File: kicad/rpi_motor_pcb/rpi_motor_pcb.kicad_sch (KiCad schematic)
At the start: 15 parts, among them J1 Raspberry_Pi_2_3, J4 PWR IN, J9 LSW1

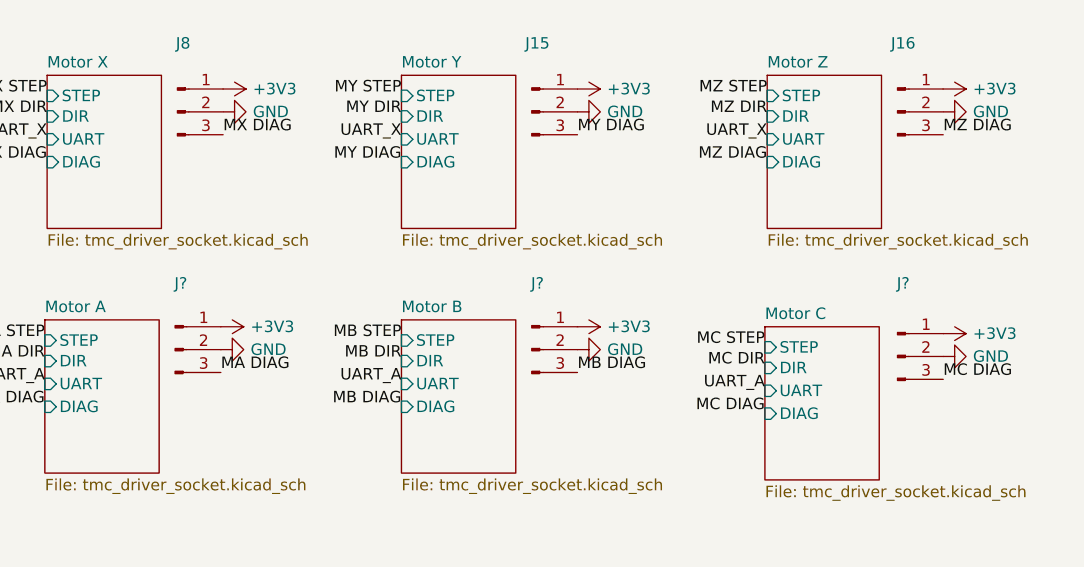
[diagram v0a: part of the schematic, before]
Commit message: rpi_motor_pcb: a,b,c endstops
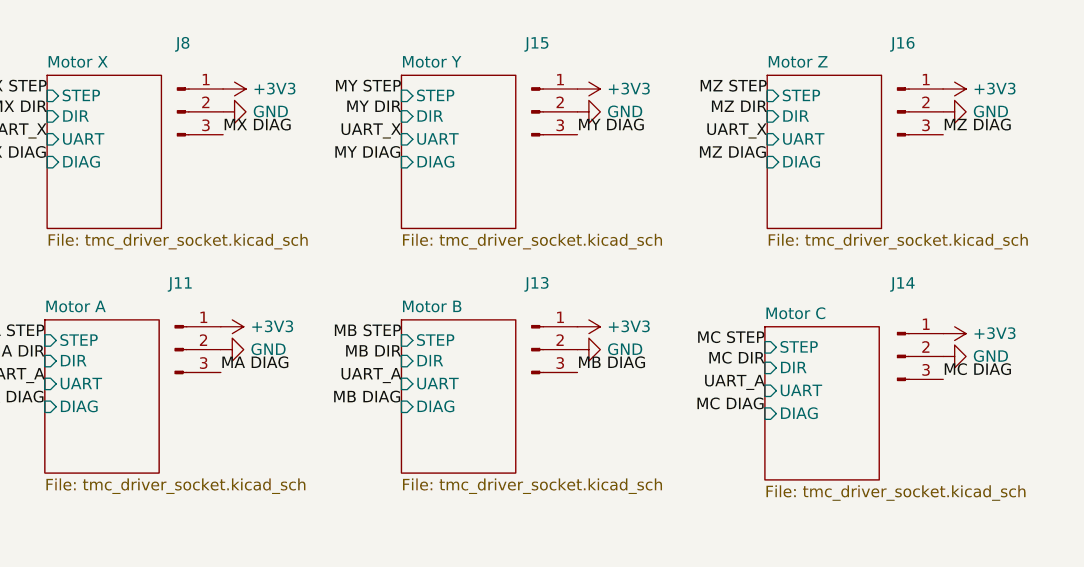
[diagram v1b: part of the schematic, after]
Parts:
- gave numbers to parts that had none: 3
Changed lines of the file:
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@@
   (symbol (lib_id "power:+3V3") (at 200.66 51.308 270) (unit 1)
     (in_bom yes) (on_board yes) (fields_autoplaced)
-    (property "Reference" "#PWR?" (id 0) (at 196.85 51.308 0)
+    (property "Reference" "#PWR091" (id 0) (at 196.85 51.308 0)
       (effects (font (size 1.27 1.27)) hide)
     )
@@
   (symbol (lib_id "power:+3V3") (at 120.396 50.546 270) (unit 1)
     (in_bom yes) (on_board yes) (fields_autoplaced)
-    (property "Reference" "#PWR?" (id 0) (at 116.586 50.546 0)
+    (property "Reference" "#PWR087" (id 0) (at 116.586 50.546 0)
       (effects (font (size 1.27 1.27)) hide)
     )
@@
   (symbol (lib_id "power:GND") (at 200.66 53.848 90) (unit 1)
     (in_bom yes) (on_board yes) (fields_autoplaced)
-    (property "Reference" "#PWR?" (id 0) (at 207.01 53.848 0)
+    (property "Reference" "#PWR092" (id 0) (at 207.01 53.848 0)
       (effects (font (size 1.27 1.27)) hide)
     )
@@
   (symbol (lib_id "power:GND") (at 160.02 53.086 90) (unit 1)
     (in_bom yes) (on_board yes) (fields_autoplaced)
-    (property "Reference" "#PWR?" (id 0) (at 166.37 53.086 0)
+    (property "Reference" "#PWR090" (id 0) (at 166.37 53.086 0)
       (effects (font (size 1.27 1.27)) hide)
     )
@@
   (symbol (lib_id "Connector:Conn_01x03_Male") (at 195.58 53.848 0) (unit 1)
     (in_bom yes) (on_board yes) (fields_autoplaced)
-    (property "Reference" "J?" (id 0) (at 196.215 45.72 0))
+    (property "Reference" "J14" (id 0) (at 196.215 45.72 0))
     (property "Value" "" (id 1) (at 196.215 48.26 0))
     (property "Footprint" "Connector_PinHeader_2.54mm:PinHeader_1x03_P2.54mm_Vertical" (id 2) (at 195.58 53.848 0)
@@
   (symbol (lib_id "power:GND") (at 120.396 53.086 90) (unit 1)
     (in_bom yes) (on_board yes) (fields_autoplaced)
-    (property "Reference" "#PWR?" (id 0) (at 126.746 53.086 0)
+    (property "Reference" "#PWR088" (id 0) (at 126.746 53.086 0)
       (effects (font (size 1.27 1.27)) hide)
     )
@@
   (symbol (lib_id "power:+3V3") (at 160.02 50.546 270) (unit 1)
     (in_bom yes) (on_board yes) (fields_autoplaced)
-    (property "Reference" "#PWR?" (id 0) (at 156.21 50.546 0)
+    (property "Reference" "#PWR089" (id 0) (at 156.21 50.546 0)
       (effects (font (size 1.27 1.27)) hide)
     )
@@
   (symbol (lib_id "Connector:Conn_01x03_Male") (at 154.94 53.086 0) (unit 1)
     (in_bom yes) (on_board yes) (fields_autoplaced)
-    (property "Reference" "J?" (id 0) (at 155.575 45.72 0))
+    (property "Reference" "J13" (id 0) (at 155.575 45.72 0))
     (property "Value" "" (id 1) (at 155.575 48.26 0))
     (property "Footprint" "Connector_PinHeader_2.54mm:PinHeader_1x03_P2.54mm_Vertical" (id 2) (at 154.94 53.086 0)
@@
   (symbol (lib_id "Connector:Conn_01x03_Male") (at 115.316 53.086 0) (unit 1)
     (in_bom yes) (on_board yes) (fields_autoplaced)
-    (property "Reference" "J?" (id 0) (at 115.951 45.72 0))
+    (property "Reference" "J11" (id 0) (at 115.951 45.72 0))
     (property "Value" "" (id 1) (at 115.951 48.26 0))
     (property "Footprint" "Connector_PinHeader_2.54mm:PinHeader_1x03_P2.54mm_Vertical" (id 2) (at 115.316 53.086 0)
@@
       (reference "#PWR086") (unit 1) (value "GND") (footprint "")
     )
+    (path "/2d37e96a-5511-4bed-b31d-e40a8cd44469"
+      (reference "#PWR087") (unit 1) (value "+3V3") (footprint "")
+    )
+    (path "/86fdbc65-ea55-4abb-bb0e-de3d715f1401"
+      (reference "#PWR088") (unit 1) (value "GND") (footprint "")
+    )
+    (path "/a9e23d65-7d04-409d-b52d-4bd1d741b888"
+      (reference "#PWR089") (unit 1) (value "+3V3") (footprint "")
+    )
+    (path "/5da43cdb-11fe-4de8-8acd-b191623db6c8"
+      (reference "#PWR090") (unit 1) (value "GND") (footprint "")
+    )
+    (path "/1dd846af-fc14-4004-9c30-d170a8887143"
+      (reference "#PWR091") (unit 1) (value "+3V3") (footprint "")
+    )
+    (path "/5b511e3c-6333-4353-9ae1-a339062409b8"
+      (reference "#PWR092") (unit 1) (value "GND") (footprint "")
+    )
     (path "/d020a2f5-1049-4c55-9a6f-82477ab73207"
       (reference "#PWR0101") (unit 1) (value "GND") (footprint "")
@@
       (reference "#PWR0124") (unit 1) (value "GND") (footprint "")
     )
-    (path "/1dd846af-fc14-4004-9c30-d170a8887143"
-      (reference "#PWR?") (unit 1) (value "+3V3") (footprint "")
-    )
-    (path "/2d37e96a-5511-4bed-b31d-e40a8cd44469"
-      (reference "#PWR?") (unit 1) (value "+3V3") (footprint "")
-    )
-    (path "/5b511e3c-6333-4353-9ae1-a339062409b8"
-      (reference "#PWR?") (unit 1) (value "GND") (footprint "")
-    )
-    (path "/5da43cdb-11fe-4de8-8acd-b191623db6c8"
-      (reference "#PWR?") (unit 1) (value "GND") (footprint "")
-    )
-    (path "/86fdbc65-ea55-4abb-bb0e-de3d715f1401"
-      (reference "#PWR?") (unit 1) (value "GND") (footprint "")
-    )
-    (path "/a9e23d65-7d04-409d-b52d-4bd1d741b888"
-      (reference "#PWR?") (unit 1) (value "+3V3") (footprint "")
-    )
     (path "/1c9edd80-85d9-4c0d-9cc6-2c3a113885ca/29c05aa4-d4e2-4af1-a60e-827ca668e338"
       (reference "A1") (unit 1) (value "${SHEETNAME} Driver") (footprint "TMCSockets:TMC220X")
@@
       (reference "J10") (unit 1) (value "CAN") (footprint "Connector_JST:JST_XH_B2B-XH-A_1x02_P2.50mm_Vertical")
     )
+    (path "/d785e888-9350-4463-a449-283195043b1b"
+      (reference "J11") (unit 1) (value "A-") (footprint "Connector_PinHeader_2.54mm:PinHeader_1x03_P2.54mm_Vertical")
+    )
     (path "/11aba65b-53a2-477d-9cee-8bb1f5f76453/f268893d-d27d-4643-8d48-d1ca2e4e5a32"
       (reference "J12") (unit 1) (value "${SHEETNAME}") (footprint "Connector_JST:JST_XH_B4B-XH-A_1x04_P2.50mm_Vertical")
     )
+    (path "/c2b3e998-9cfe-4c9e-a7b7-60356a7de733"
+      (reference "J13") (unit 1) (value "B-") (footprint "Connector_PinHeader_2.54mm:PinHeader_1x03_P2.54mm_Vertical")
+    )
+    (path "/855a6ed4-b488-4169-b98e-aca2285b8954"
+      (reference "J14") (unit 1) (value "C-") (footprint "Connector_PinHeader_2.54mm:PinHeader_1x03_P2.54mm_Vertical")
+    )
     (path "/15adfdb7-0a96-47d8-b1f2-e517a0c7adc2"
       (reference "J15") (unit 1) (value "Y-") (footprint "Connector_PinHeader_2.54mm:PinHeader_1x03_P2.54mm_Vertical")
@@
       (reference "J18") (unit 1) (value "${SHEETNAME}") (footprint "Connector_JST:JST_XH_B2B-XH-A_1x02_P2.50mm_Vertical")
     )
-    (path "/855a6ed4-b488-4169-b98e-aca2285b8954"
-      (reference "J?") (unit 1) (value "C-") (footprint "Connector_PinHeader_2.54mm:PinHeader_1x03_P2.54mm_Vertical")
-    )
-    (path "/c2b3e998-9cfe-4c9e-a7b7-60356a7de733"
-      (reference "J?") (unit 1) (value "B-") (footprint "Connector_PinHeader_2.54mm:PinHeader_1x03_P2.54mm_Vertical")
-    )
-    (path "/d785e888-9350-4463-a449-283195043b1b"
-      (reference "J?") (unit 1) (value "A-") (footprint "Connector_PinHeader_2.54mm:PinHeader_1x03_P2.54mm_Vertical")
-    )
     (path "/1c9edd80-85d9-4c0d-9cc6-2c3a113885ca/a006615d-32f1-4530-8f68-5161c2fe10b0"

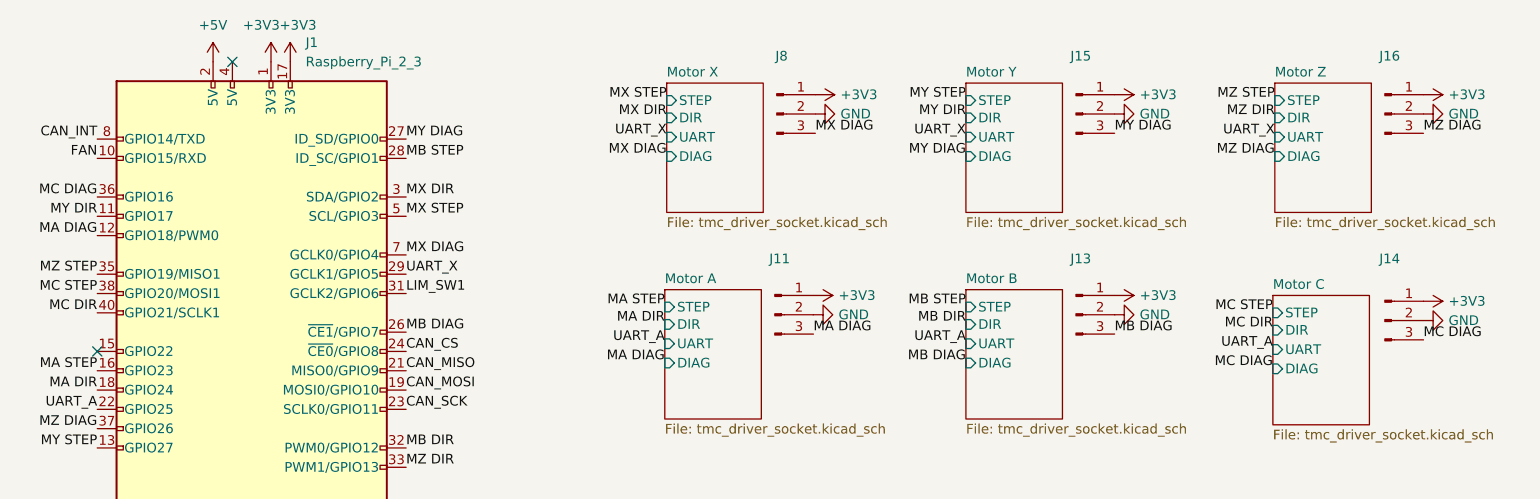
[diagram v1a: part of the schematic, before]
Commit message: rpi_motor_pcb: 6-axis fix diag pin, add en pin
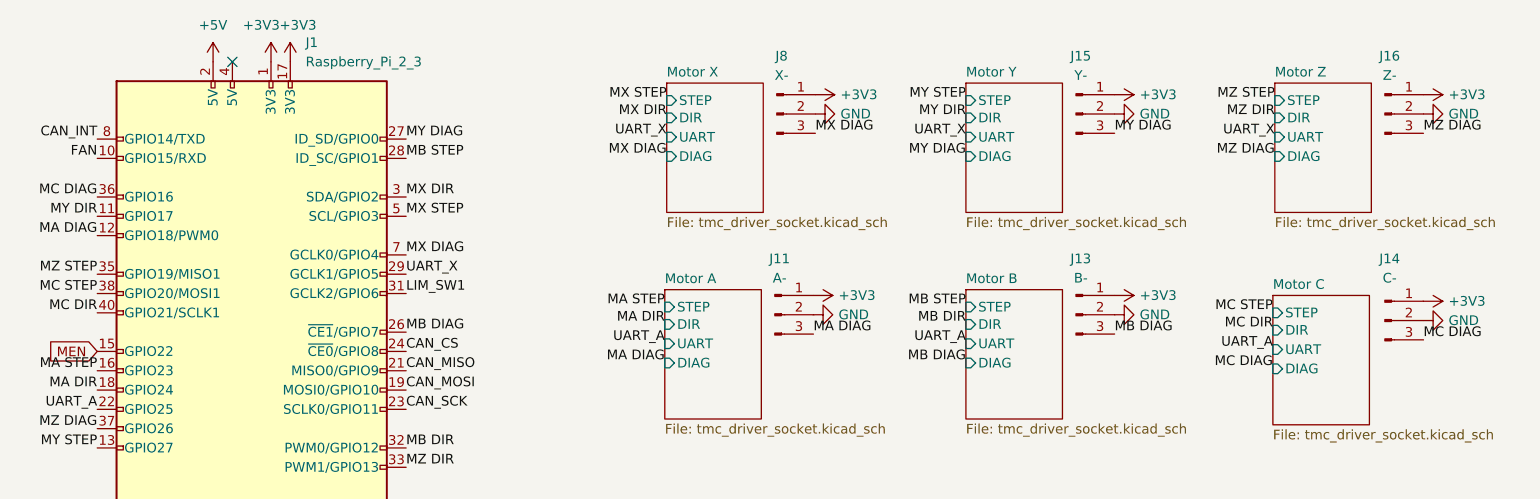
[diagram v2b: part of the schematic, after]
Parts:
- J11: value (none) -> A-
- J13: value (none) -> B-
- J14: value (none) -> C-
- J15: value (none) -> Y-
- J16: value (none) -> Z-
- J8: value (none) -> X-
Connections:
- net MEN: now reaches J1.15 (GPIO22)
- no-connect marks 5 -> 4
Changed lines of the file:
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@@
   (no_connect (at 41.402 85.852))
   (no_connect (at 36.322 85.852))
-  (no_connect (at 26.162 57.912))
   (no_connect (at 38.862 85.852))
   (wire (pts (xy 51.562 85.852) (xy 54.102 85.852))
@@
     )
   )
+  (global_label "MEN" (shape input) (at 26.162 57.912 180) (fields_autoplaced)
+    (effects (font (size 1.27 1.27)) (justify right))
+    (property "Intersheet References" "${INTERSHEET_REFS}" (id 0) (at 19.8179 57.8326 0)
+      (effects (font (size 1.27 1.27)) (justify right) hide)
+    )
+  )
   (global_label "Vin" (shape input) (at 234.442 151.384 90) (fields_autoplaced)
     (effects (font (size 1.27 1.27)) (justify left))
@@
     (in_bom yes) (on_board yes) (fields_autoplaced)
     (property "Reference" "J15" (id 0) (at 155.575 19.05 0))
-    (property "Value" "" (id 1) (at 155.575 21.59 0))
+    (property "Value" "Y-" (id 1) (at 155.575 21.59 0))
     (property "Footprint" "Connector_PinHeader_2.54mm:PinHeader_1x03_P2.54mm_Vertical" (id 2) (at 154.94 26.67 0)
       (effects (font (size 1.27 1.27)) hide)
@@
     (in_bom yes) (on_board yes) (fields_autoplaced)
     (property "Reference" "J8" (id 0) (at 116.205 19.05 0))
-    (property "Value" "" (id 1) (at 116.205 21.59 0))
+    (property "Value" "X-" (id 1) (at 116.205 21.59 0))
     (property "Footprint" "Connector_PinHeader_2.54mm:PinHeader_1x03_P2.54mm_Vertical" (id 2) (at 115.57 26.67 0)
       (effects (font (size 1.27 1.27)) hide)
@@
     (in_bom yes) (on_board yes) (fields_autoplaced)
     (property "Reference" "J14" (id 0) (at 196.215 45.72 0))
-    (property "Value" "" (id 1) (at 196.215 48.26 0))
+    (property "Value" "C-" (id 1) (at 196.215 48.26 0))
     (property "Footprint" "Connector_PinHeader_2.54mm:PinHeader_1x03_P2.54mm_Vertical" (id 2) (at 195.58 53.848 0)
       (effects (font (size 1.27 1.27)) hide)
@@
     (in_bom yes) (on_board yes) (fields_autoplaced)
     (property "Reference" "J16" (id 0) (at 196.215 19.05 0))
-    (property "Value" "" (id 1) (at 196.215 21.59 0))
+    (property "Value" "Z-" (id 1) (at 196.215 21.59 0))
     (property "Footprint" "Connector_PinHeader_2.54mm:PinHeader_1x03_P2.54mm_Vertical" (id 2) (at 195.58 26.67 0)
       (effects (font (size 1.27 1.27)) hide)
@@
     (in_bom yes) (on_board yes) (fields_autoplaced)
     (property "Reference" "J13" (id 0) (at 155.575 45.72 0))
-    (property "Value" "" (id 1) (at 155.575 48.26 0))
+    (property "Value" "B-" (id 1) (at 155.575 48.26 0))
     (property "Footprint" "Connector_PinHeader_2.54mm:PinHeader_1x03_P2.54mm_Vertical" (id 2) (at 154.94 53.086 0)
       (effects (font (size 1.27 1.27)) hide)
@@
     (in_bom yes) (on_board yes) (fields_autoplaced)
     (property "Reference" "J11" (id 0) (at 115.951 45.72 0))
-    (property "Value" "" (id 1) (at 115.951 48.26 0))
+    (property "Value" "A-" (id 1) (at 115.951 48.26 0))
     (property "Footprint" "Connector_PinHeader_2.54mm:PinHeader_1x03_P2.54mm_Vertical" (id 2) (at 115.316 53.086 0)
       (effects (font (size 1.27 1.27)) hide)
@@
       (reference "#PWR03") (unit 1) (value "GND") (footprint "")
     )
-    (path "/2f97629b-ca35-40e1-950a-976dc6d5099e/8d7dffa6-e4ab-477e-b14a-0cd63cbed4e0"
-      (reference "#PWR04") (unit 1) (value "GND") (footprint "")
-    )
     (path "/2f97629b-ca35-40e1-950a-976dc6d5099e/7e0b5e6c-5e10-4bbc-b043-eb819dc2cf4f"
       (reference "#PWR05") (unit 1) (value "+3V3") (footprint "")
@@
       (reference "#PWR010") (unit 1) (value "GND") (footprint "")
     )
-    (path "/cbfe036f-5613-48df-a314-10875a3b599a/8d7dffa6-e4ab-477e-b14a-0cd63cbed4e0"
-      (reference "#PWR011") (unit 1) (value "GND") (footprint "")
-    )
     (path "/cbfe036f-5613-48df-a314-10875a3b599a/7e0b5e6c-5e10-4bbc-b043-eb819dc2cf4f"
       (reference "#PWR012") (unit 1) (value "+3V3") (footprint "")
@@
       (reference "#PWR015") (unit 1) (value "GND") (footprint "")
     )
-    (path "/21d5a0dd-8380-4cbc-877d-09f4ecd37e4d/8d7dffa6-e4ab-477e-b14a-0cd63cbed4e0"
-      (reference "#PWR016") (unit 1) (value "GND") (footprint "")
-    )
     (path "/21d5a0dd-8380-4cbc-877d-09f4ecd37e4d/7e0b5e6c-5e10-4bbc-b043-eb819dc2cf4f"
       (reference "#PWR017") (unit 1) (value "+3V3") (footprint "")
@@
       (reference "#PWR020") (unit 1) (value "GND") (footprint "")
     )
-    (path "/19bc01f1-ddb0-42eb-b5a4-99228b6f4f71/8d7dffa6-e4ab-477e-b14a-0cd63cbed4e0"
-      (reference "#PWR021") (unit 1) (value "GND") (footprint "")
-    )
     (path "/19bc01f1-ddb0-42eb-b5a4-99228b6f4f71/7e0b5e6c-5e10-4bbc-b043-eb819dc2cf4f"
       (reference "#PWR022") (unit 1) (value "+3V3") (footprint "")
@@
       (reference "#PWR025") (unit 1) (value "GND") (footprint "")
     )
-    (path "/11aba65b-53a2-477d-9cee-8bb1f5f76453/8d7dffa6-e4ab-477e-b14a-0cd63cbed4e0"
-      (reference "#PWR026") (unit 1) (value "GND") (footprint "")
-    )
     (path "/11aba65b-53a2-477d-9cee-8bb1f5f76453/7e0b5e6c-5e10-4bbc-b043-eb819dc2cf4f"
       (reference "#PWR027") (unit 1) (value "+3V3") (footprint "")
@@
       (reference "#PWR0111") (unit 1) (value "GND") (footprint "")
     )
-    (path "/1c9edd80-85d9-4c0d-9cc6-2c3a113885ca/8d7dffa6-e4ab-477e-b14a-0cd63cbed4e0"
-      (reference "#PWR0112") (unit 1) (value "GND") (footprint "")
-    )
     (path "/d69eafbd-851d-4c7c-b105-d4f0f64cd6e5"
